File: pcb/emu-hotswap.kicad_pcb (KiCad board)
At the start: 2 copper layers, 157.6 x 118.1 mm, 77 parts, among them J1 TRRS, SW1 SW_Push, SW10 SW_Push, SW11 SW_Push, SW12 SW_Push, SW13 SW_Push, SW14 SW_Push, SW15 SW_Push, SW16 SW_Push, SW17 SW_Push, SW18 SW_Push, SW19 SW_Push, SW2 SW_Push, SW20 SW_Push, SW21 SW_Push, SW22 SW_Push, SW23 SW_Push, SW24 SW_Push, SW25 SW_Push, SW26 SW_Push, SW27 SW_Push, SW28 SW_Push, SW29 SW_Push, SW3 SW_Push, SW30 SW_Push, SW31 SW_Push, SW32 SW_Push, SW4 SW_Push, SW5 SW_Push, SW6 SW_Push, SW7 SW_Push, SW8 SW_Push, SW9 SW_Push, U1 ProMicro

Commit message: Started new simple and weird design.
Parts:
- removed U1: ProMicro, used_footprints:ArduinoProMicro_dual
- added REF**: ProMicro_Dual, used_footprints:ProMicro_Dual, F.Cu at (244.4, 76.4)
- moved HM3 42.2 mm to (241.9, 106.2)
- moved D7 19.7 mm to (124.0, 75.5)
- moved R2 6.85 mm to (215.2, 68.9), turned to 279 degrees
- moved J1 6.68 mm to (224.2, 58.3), turned to 9 degrees
- moved R1 5.94 mm to (218.5, 68.4), turned to 279 degrees
- moved D2 5.84 mm to (105.0, 75.5)
- moved JP3 5.42 mm to (228.6, 72.5), turned to 189 degrees
- moved JP4 5.42 mm to (228.6, 72.5), turned to 189 degrees
- moved SW32 4.97 mm to (215.3, 59.5), turned to 9 degrees
- moved JP1 4.86 mm to (224.5, 73.2), turned to 189 degrees
- moved JP2 4.86 mm to (224.5, 73.2), turned to 189 degrees
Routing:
- net GND: track 200.3 -> 4.85 mm, vias 3 -> 0
- net SCL: track 200.2 -> 16.3 mm, vias 3 -> 1
- net /rowF: track 196.1 -> 14.6 mm, vias 4 -> 0
- net /rowC: track 258.4 -> 82.6 mm, vias 2 -> 0
- net SDA: track 183.4 -> 7.51 mm, vias 3 -> 1
- net VCC: track 165.0 -> 6.74 mm, vias 1 -> 0
- net /rowB: track 181.3 -> 41.3 mm, vias 2 -> 0
- net /RST: track 144.8 -> 16.5 mm, vias 2 -> 0
- net /col5: track 314.4 -> 201.3 mm, vias 8 -> 6
- net /col4: track 307.4 -> 200.9 mm, vias 7 -> 5
- net /col1: track 258.2 -> 167.8 mm, vias 7 -> 3
- net /col3: track 271.7 -> 199.6 mm, vias 8 -> 5
- net /col2: track 239.0 -> 171.9 mm, vias 6 -> 4
- net /col0: track 163.9 -> 112.5 mm, vias 4 -> 2
- net Net-(D2-Pad2): track 37.6 -> 0.00 mm, vias 3 -> 0
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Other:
- board size 157.6 x 118.1 mm -> 180.2 x 118.1 mm

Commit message: Routing...
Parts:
- removed REF**: ProMicro_Dual, used_footprints:ProMicro_Dual
- added U1: ProMicro, used_footprints:ProMicro_Dual, F.Cu at (244.5, 76.5)
- moved HM5 1.03 mm to (95.5, 98.6)
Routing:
- net /col0: track 112.5 -> 312.6 mm, vias 2 -> 8
- net /col1: track 167.8 -> 328.3 mm, vias 3 -> 7
- net /col2: track 171.9 -> 296.3 mm, vias 4 -> 6
- net /col3: track 199.6 -> 315.0 mm, vias 5 -> 8
- net /rowB: track 41.3 -> 150.0 mm, vias 0 -> 1
- net /col4: track 200.9 -> 274.9 mm, vias 5 -> 6
- net /rowC: track 82.6 -> 144.9 mm
- net GND: track 4.85 -> 49.8 mm, vias 0 -> 2
- net Net-(D2-Pad2): track 0.00 -> 28.6 mm
- net Net-(D7-Pad2): track 0.00 -> 28.0 mm
- net /col5: track 201.3 -> 225.3 mm, vias 6 -> 7
- net SCL: track 16.3 -> 33.4 mm, vias 1 -> 2
- net /rowA: track 133.0 -> 150.0 mm, vias 0 -> 1
- net SDA: track 7.51 -> 24.6 mm, vias 1 -> 2
- net Net-(U1-Pad15): track 0.00 -> 14.4 mm
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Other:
- outline, holes or cut-outs redrawn

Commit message: Routing...
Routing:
- net /rowA: track 150.0 -> 228.9 mm, vias 1 -> 2
- net /rowD: track 151.8 -> 223.3 mm, vias 0 -> 1
- net /rowB: track 150.0 -> 217.4 mm, vias 1 -> 3
- net /rowE: track 206.6 -> 263.0 mm, vias 0 -> 1
- net /rowC: track 144.9 -> 187.2 mm, vias 0 -> 2
- net GND: track 49.8 -> 83.1 mm, vias 2 -> 3
- net SCL: track 33.4 -> 62.9 mm
- net /rowF: track 18.8 -> 47.8 mm, vias 0 -> 1
- net /RST: track 14.4 -> 41.9 mm, vias 0 -> 1
- net VCC: track 21.2 -> 48.6 mm
- net SDA: track 24.6 -> 44.0 mm, vias 2 -> 3
- net Net-(D12-Pad2): track 15.3 -> 27.9 mm
- net Net-(D13-Pad2): track 18.5 -> 27.9 mm
- net /col2: track 296.3 -> 297.3 mm
- net /col5: track 225.3 -> 224.8 mm, vias 7 -> 8
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
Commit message: Routing is done.
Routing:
- net /col1: track 328.8 -> 325.9 mm

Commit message: Holes.
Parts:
- added HM10: CaseHole, used_footprints:Hole_Mount_M4, F.Cu at (190.8, 74.8)
- added HM11: CaseHole, used_footprints:Hole_Mount_M4, F.Cu at (152.7, 68.5)
- added HM12: CaseHole, used_footprints:Hole_Mount_M4, F.Cu at (234.0, 45.2)
- added HM7: CaseHole, used_footprints:Hole_Mount_M4, F.Cu at (114.5, 60.5)
- added HM8: CaseHole, used_footprints:Hole_Mount_M4, F.Cu at (114.5, 79.6)
- added HM9: CaseHole, used_footprints:Hole_Mount_M4, F.Cu at (152.7, 49.5)
- moved HM2 59.5 mm to (190.8, 55.8)
- moved HM4 5.53 mm to (164.3, 115.9)
- moved HM3 3.43 mm to (240.8, 109.5)
- moved R1 2.23 mm to (216.3, 68.9), turned to 270 degrees
- moved R2 2.22 mm to (213.0, 68.9), turned to 270 degrees
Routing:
- net SCL: track 62.9 -> 68.7 mm
- net SDA: track 44.0 -> 46.5 mm
- net VCC: track 48.6 -> 50.3 mm

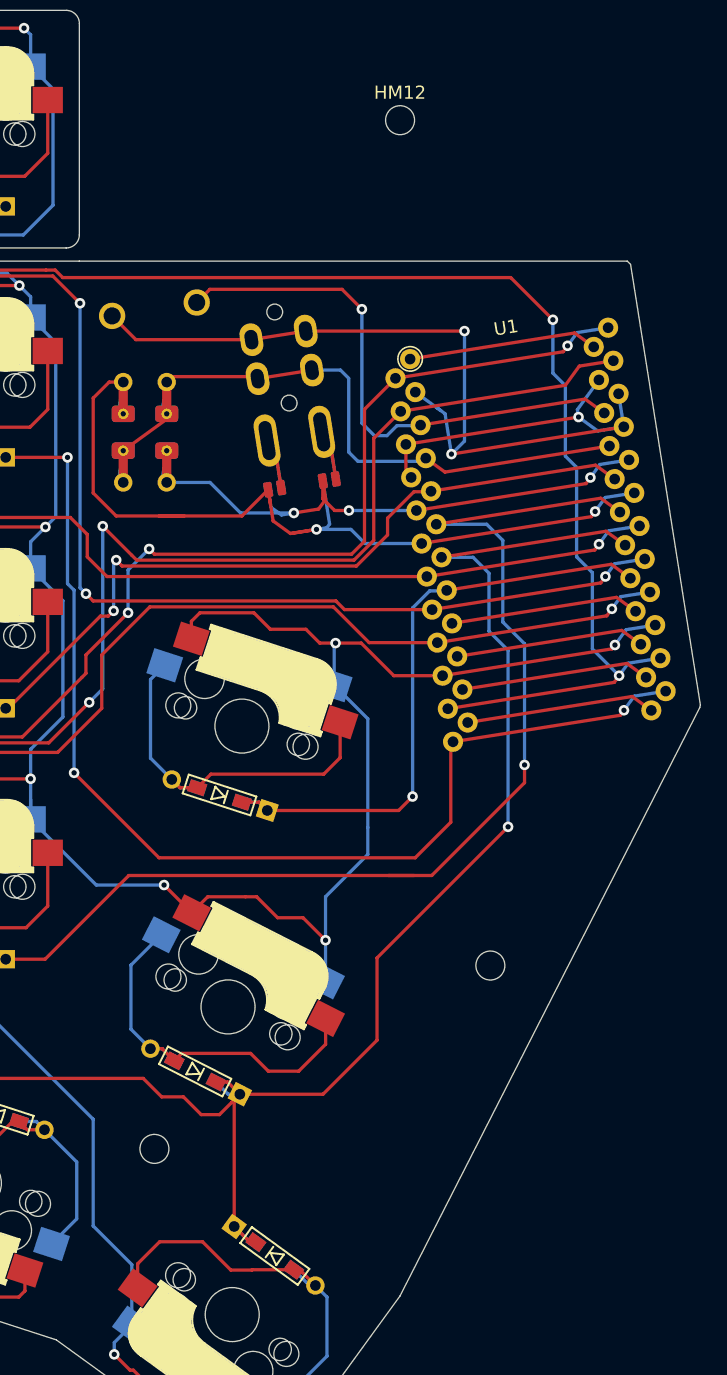
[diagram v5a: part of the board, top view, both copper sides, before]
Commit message: Curved cut.
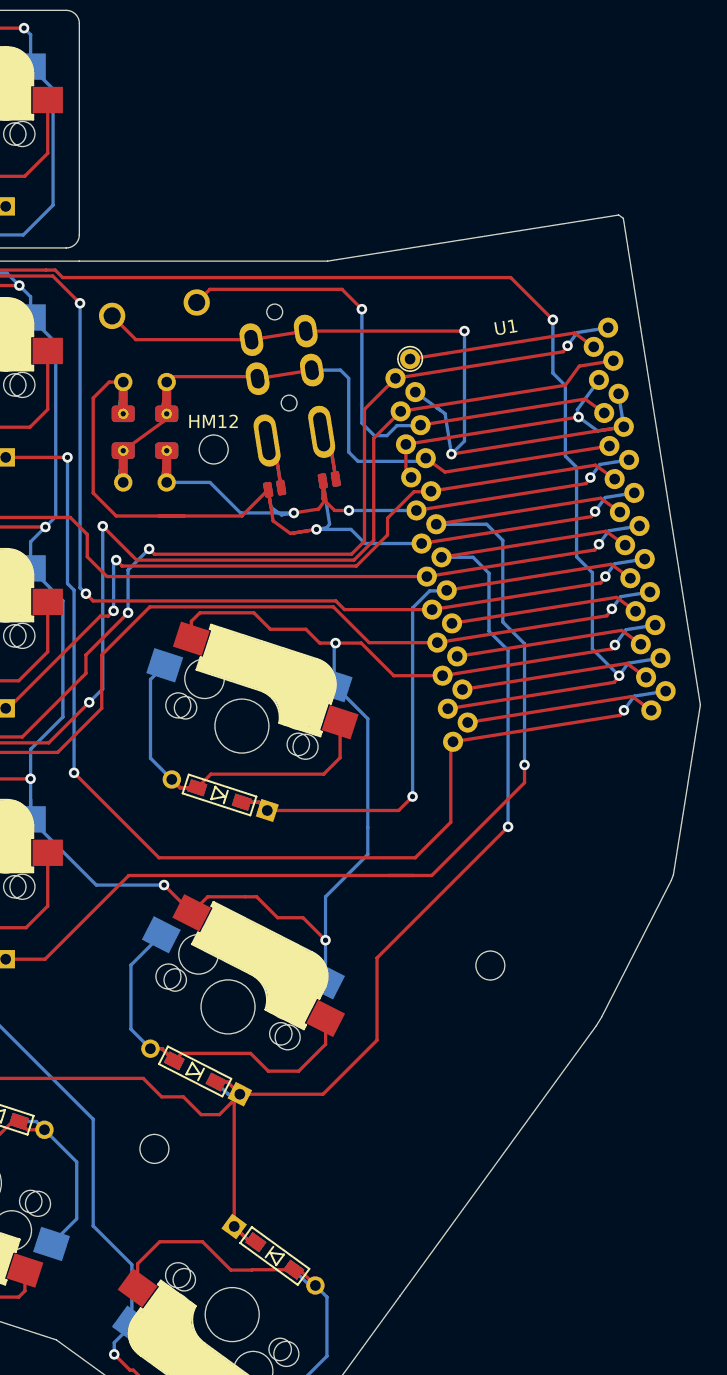
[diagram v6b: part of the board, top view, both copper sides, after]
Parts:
- moved HM12 28.7 mm to (219.8, 70.2)
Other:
- outline, holes or cut-outs redrawn

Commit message: Re-routing.
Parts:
- moved U1 3.25 mm to (243.9, 73.3)
- turned SW32 to 0 degrees
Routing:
- net /col1: track 325.9 -> 329.9 mm
- net VCC: track 50.3 -> 46.5 mm
- net /RST: track 41.9 -> 38.4 mm
- net /rowE: track 263.0 -> 266.4 mm
- net /rowC: track 187.2 -> 190.2 mm
- net /col0: track 312.6 -> 315.6 mm
- net /rowF: track 47.8 -> 50.1 mm
- net /rowA: track 228.9 -> 227.0 mm
- net GND: track 83.1 -> 84.7 mm
- net /col4: track 274.9 -> 273.4 mm
- net /rowB: track 217.4 -> 218.8 mm
- net /col5: track 224.8 -> 223.5 mm
- net /col2: track 297.3 -> 298.0 mm
- net SDA: track 46.5 -> 47.3 mm
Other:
- outline, holes or cut-outs redrawn

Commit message: Top Plate
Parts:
- moved HM12 1.03 mm to (220.1, 69.2)
- moved J1 0.55 mm to (224.7, 58.6)
- moved JP1 0.55 mm to (224.9, 73.5)
- moved JP2 0.55 mm to (224.9, 73.5)
- moved JP3 0.55 mm to (229.1, 72.8)
- moved JP4 0.55 mm to (229.1, 72.8)
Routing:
- net SCL: track 68.6 -> 71.6 mm
- net SDA: track 47.3 -> 44.9 mm
- net GND: track 84.7 -> 86.1 mm
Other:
- outline, holes or cut-outs redrawn
